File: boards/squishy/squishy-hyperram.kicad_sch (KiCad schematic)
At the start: 3 parts, among them U19 HyperRAM

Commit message: hardware: squishy: minor updates
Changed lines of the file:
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@@
     (effects (font (size 1.27 1.27)) (justify right bottom))
+  )
+  (hierarchical_label "RAM{HR}" (shape bidirectional) (at 74.93 83.82 180)
+    (effects (font (size 1.27 1.27)) (justify right))
   )
   (symbol (lib_id "Device:R_Small") (at 179.07 83.82 0) (unit 1)

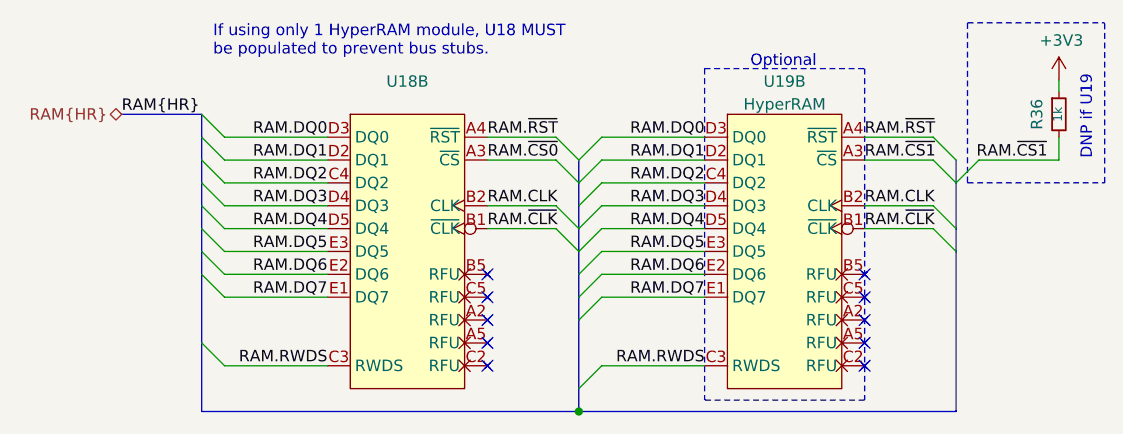
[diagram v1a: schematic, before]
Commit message: hardware: some minor rev2 updates, mainly hyperram
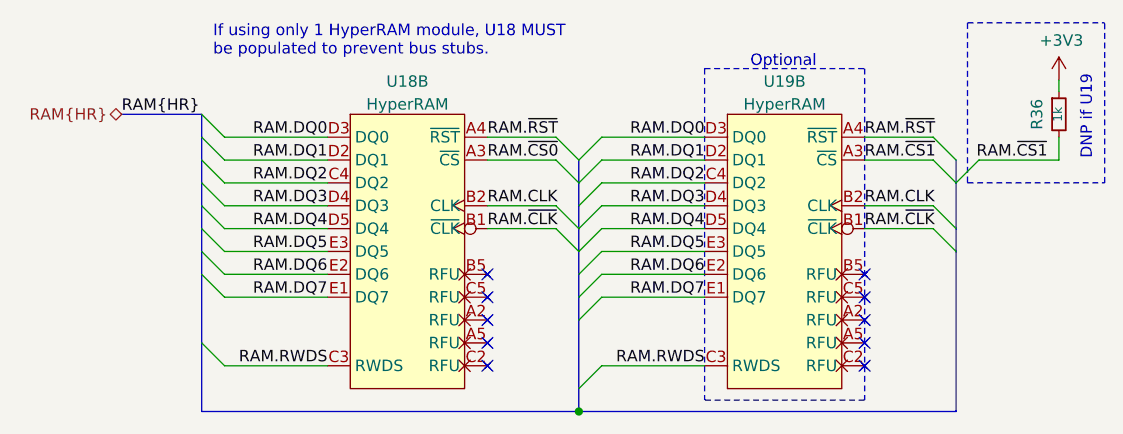
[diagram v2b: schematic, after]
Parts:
- U18: value (none) -> HyperRAM; footprint (none) -> lethalbit-memory:TFBGA-24-6x8mm-1.0mm
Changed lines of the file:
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@@
     (in_bom yes) (on_board yes) (fields_autoplaced)
     (property "Reference" "U18" (id 0) (at 106.68 80.171 0))
-    (property "Value" "" (id 1) (at 106.68 82.7079 0))
-    (property "Footprint" "" (id 2) (at 106.68 85.09 0)
+    (property "Value" "HyperRAM" (id 1) (at 106.68 82.7079 0))
+    (property "Footprint" "lethalbit-memory:TFBGA-24-6x8mm-1.0mm" (id 2) (at 106.68 85.09 0)
       (effects (font (size 1.27 1.27)) hide)
     )
